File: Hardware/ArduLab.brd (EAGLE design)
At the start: 80 x 100 mm, 92 parts, among them CN1 USB-B, CN2 JST-PH, Q1 BSS138, Q2 BSS138, U1 ATMEGA32U4-AU, U2 MIC5205, U3 PAM2401, U4 MCP73831, U5 L293DD, U6 HC_05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

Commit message: Added R23 (100k) as optional resistor for inductor current limit
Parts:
- added R23: 100k, resistor:R1206
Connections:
- new net N$7: R23.1, U3.6
- net GND: now also R23.2
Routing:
- net N$7: track 0.00 -> 7.60 mm, vias 0 -> 1

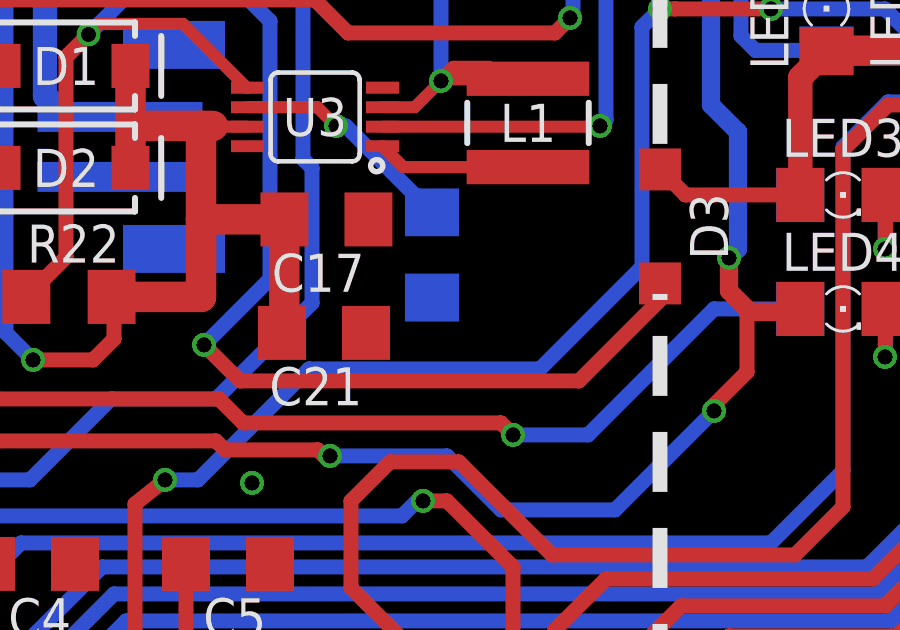
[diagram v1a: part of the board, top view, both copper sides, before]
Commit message: Added PTC reset fuse 6V 500mA. Package 1206. Part number: 1206L050YR
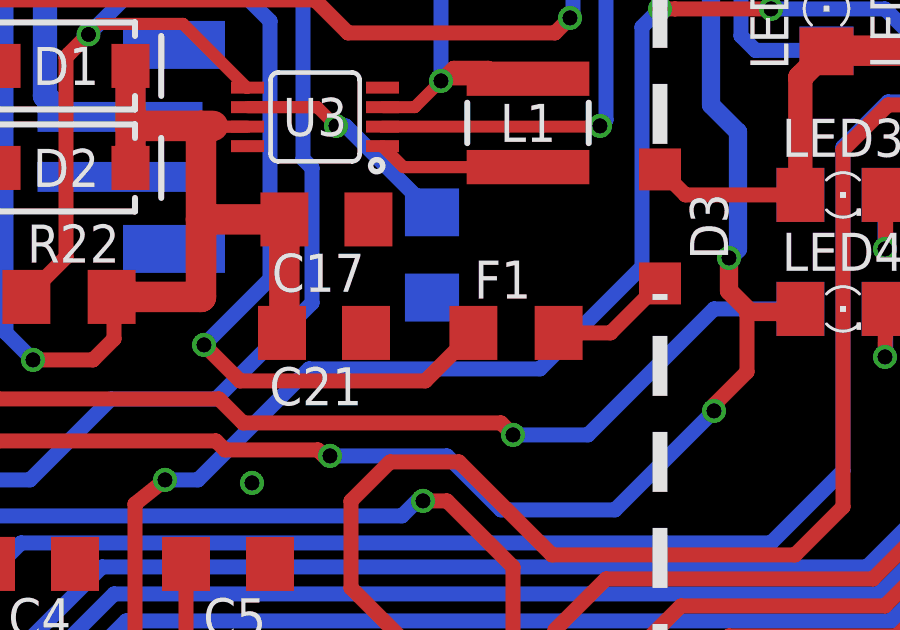
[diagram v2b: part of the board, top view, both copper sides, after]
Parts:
- added F1: 500mA, adafruit:R1206
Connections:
- new net N$15: D3.A, F1.2
- net N$3: now also F1.1; no longer D3.A
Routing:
- net N$3: track 47.1 -> 39.9 mm
- net N$15: track 0.00 -> 4.06 mm
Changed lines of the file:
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@@
 <element name="D3" library="diode" package="SOD123" value="MBR120" x="56" y="79.25" rot="R270"/>
 <element name="R23" library="resistor" package="R1206" value="100k" x="48.4" y="78.3" rot="MR270"/>
+<element name="F1" library="adafruit" package="R1206" value="500mA" x="51.2" y="75.7"/>
 </elements>
 <signals>
@@
 </signal>
 <signal name="N$3">
-<contactref element="D3" pad="A"/>
 <contactref element="S1" pad="5"/>
-<wire x1="56" y1="77.35" x2="56" y2="76.8" width="0.5" layer="1"/>
-<wire x1="56" y1="76.8" x2="53.3" y2="74.1" width="0.5" layer="1"/>
-<wire x1="53.3" y1="74.1" x2="42" y2="74.1" width="0.5" layer="1"/>
 <wire x1="42" y1="74.1" x2="40.8" y2="75.3" width="0.5" layer="1"/>
 <via x="40.8" y="75.3" extent="1-16" drill="0.5"/>
@@
 <wire x1="38.5" y1="97" x2="38" y2="97.5" width="0.5" layer="16"/>
 <wire x1="38" y1="97.5" x2="38" y2="98.651" width="0.5" layer="16"/>
+<contactref element="F1" pad="1"/>
+<wire x1="42" y1="74.1" x2="48.178" y2="74.1" width="0.5" layer="1"/>
+<wire x1="48.178" y1="74.1" x2="49.778" y2="75.7" width="0.5" layer="1"/>
 </signal>
 <signal name="N$7">
@@
 <wire x1="45.522" y1="82.6" x2="48.4" y2="79.722" width="0.5" layer="16"/>
 </signal>
+<signal name="N$15">
+<contactref element="D3" pad="A"/>
+<contactref element="F1" pad="2"/>
+<wire x1="52.622" y1="75.7" x2="54.35" y2="75.7" width="0.5" layer="1"/>
+<wire x1="54.35" y1="75.7" x2="56" y2="77.35" width="0.5" layer="1"/>
+</signal>
 </signals>

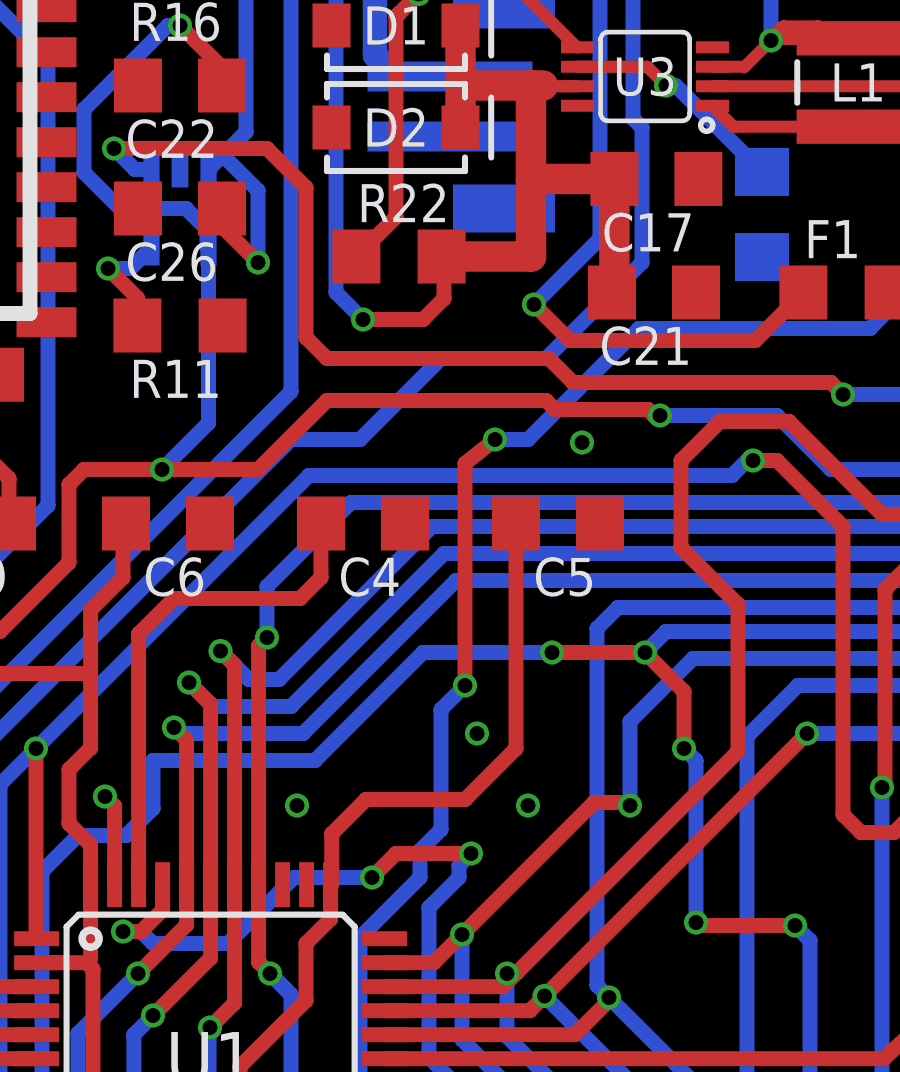
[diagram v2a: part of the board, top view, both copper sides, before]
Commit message: Connection between pin A0 and battery voltage pin for monitoring the battery status.
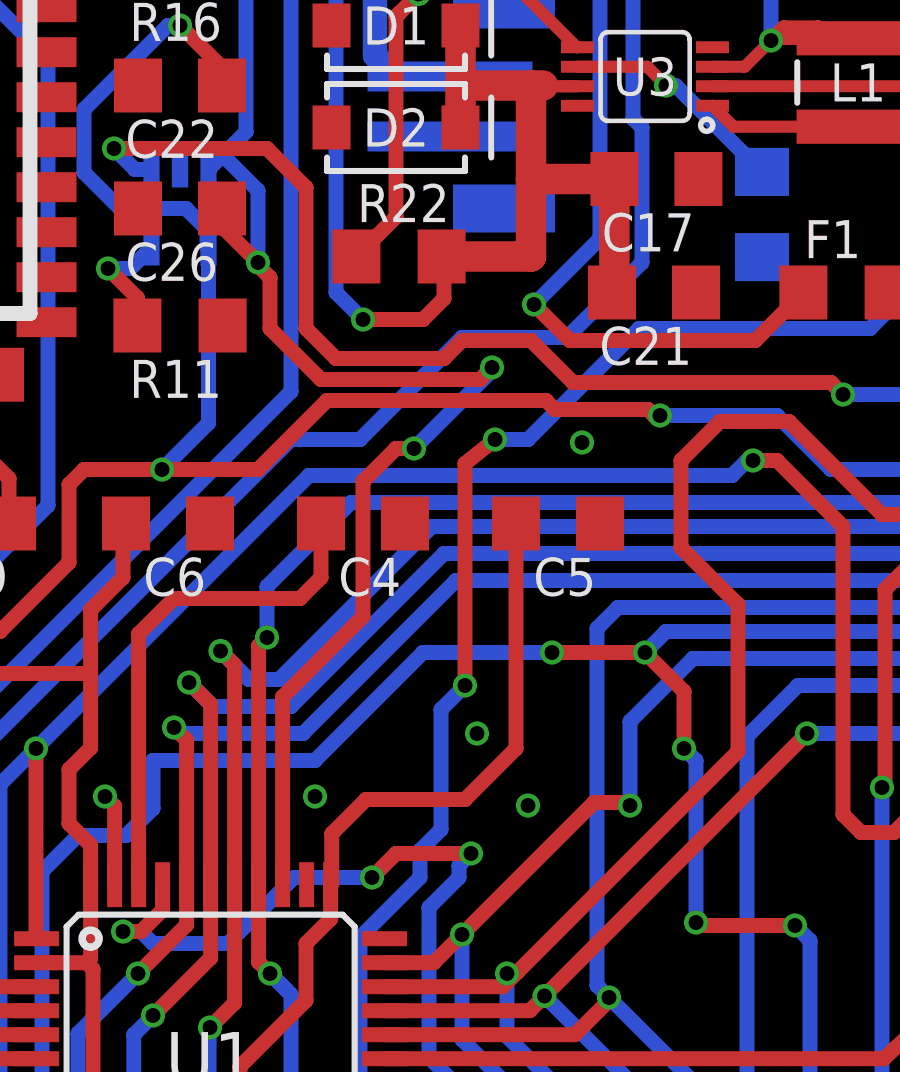
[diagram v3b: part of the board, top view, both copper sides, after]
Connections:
- removed net A0: U1.36
- net VIN: now also U1.36
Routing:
- net VIN: track 69.0 -> 100.1 mm, vias 4 -> 6

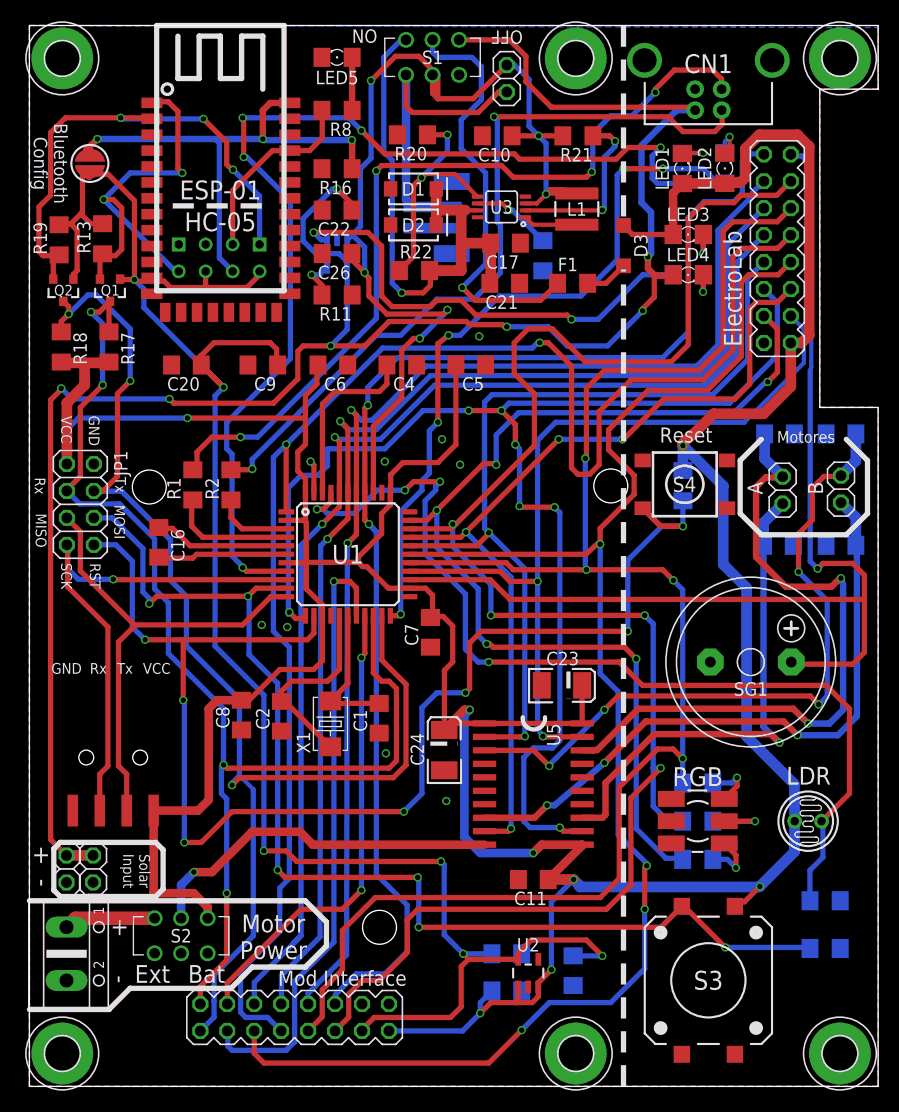
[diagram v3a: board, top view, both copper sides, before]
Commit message: 2.4GHz RF ML01D Module Integration
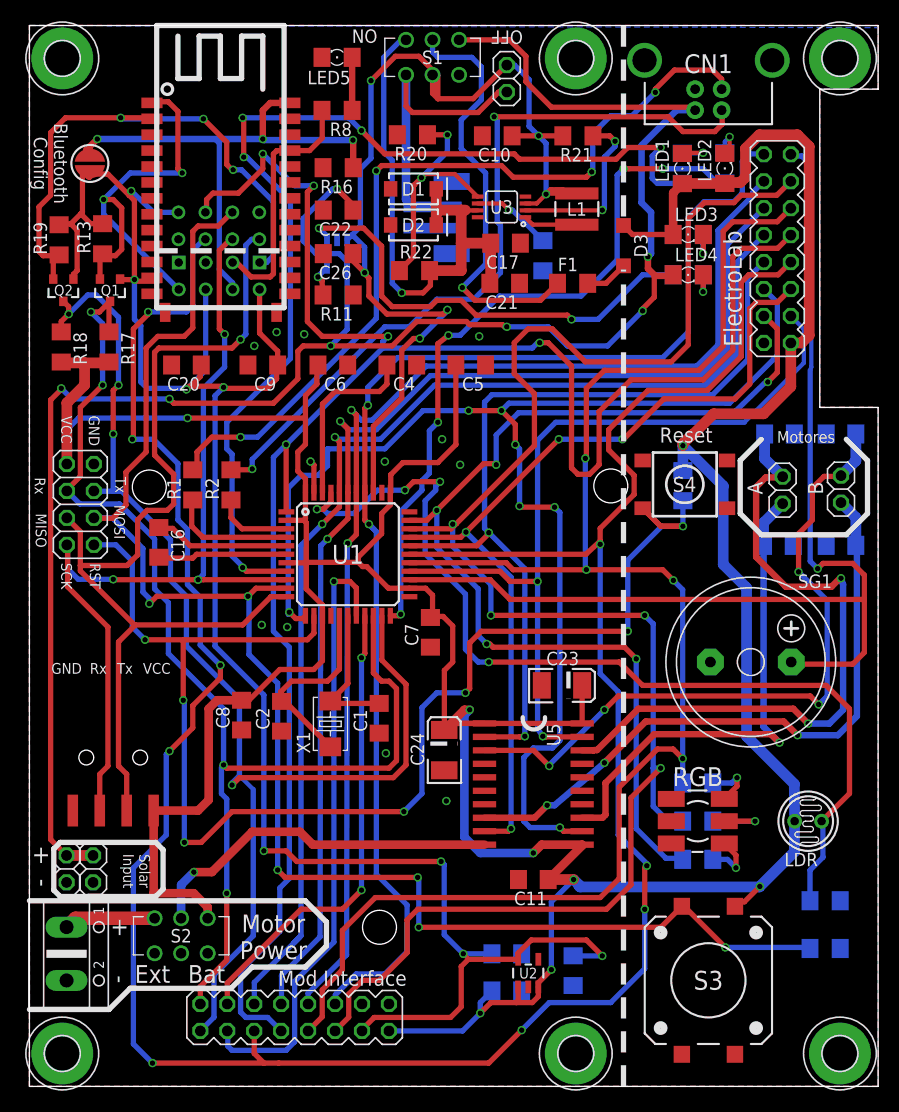
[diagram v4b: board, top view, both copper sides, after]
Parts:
- added U$2: E01-ML01D, SpaceDIY_connectors:E01-ML01D
- moved U$1 1.70 mm to (17.9, 83.3)
- moved R16 0.14 mm to (29.1, 86.6)
- moved C22 0.10 mm to (29.1, 82.6)
- moved C26 0.10 mm to (29.1, 78.5)
- moved R11 0.10 mm to (29.1, 74.6)
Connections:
- net 3.3V: now also U$2.P$2
- net D14: now also U$2.P$7
- net D15: now also U$2.P$5
- net D16: now also U$2.P$6
- net D7: now also U$2.P$4
- net D8: now also U$2.P$3
- net GND: now also U$2.P$1
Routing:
- net D8: track 144.4 -> 246.3 mm, vias 4 -> 9
- net D14: track 46.8 -> 94.2 mm, vias 0 -> 1
- net D16: track 109.5 -> 147.4 mm
- net D7: track 147.2 -> 184.9 mm, vias 2 -> 5
- net D15: track 50.3 -> 84.2 mm, vias 1 -> 3
- net 3.3V: track 186.1 -> 195.3 mm, vias 6 -> 8
- net CL: track 18.2 -> 23.7 mm
- net RX: track 48.7 -> 52.4 mm
- net D1: track 122.5 -> 120.4 mm, vias 3 -> 4
- net CONF: track 47.2 -> 48.9 mm
- net TX: track 37.7 -> 39.3 mm
- net N$10: track 4.05 -> 3.10 mm
- net GND: vias 9 -> 12
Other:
- board text removed: "ESP-01"
- board text removed: "HC-05"
